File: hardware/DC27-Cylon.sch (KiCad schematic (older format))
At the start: 32 parts, among them J1 CONN_04LOCK, J2 CONN_05LOCK, U1 STM32F030K6Tx, U2 AZ1117-3.3, Y1 16MHz

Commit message: some fixes for fab
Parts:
- C1, C2, C3, C4, C5: footprint Capacitors_SMD:C_0603 -> Sparkfun_Capacitors:0603
- U2: footprint Digikey:SOT-23-3 -> Package_TO_SOT_SMD:SOT-223-3_TabPin2
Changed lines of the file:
@@
 F 0 "C3" H 1365 1396 50  0000 L CNN
 F 1 "22p" H 1365 1305 50  0000 L CNN
-F 2 "Capacitors_SMD:C_0603" H 1288 1200 50  0001 C CNN
+F 2 "Sparkfun_Capacitors:0603" H 1288 1200 50  0001 C CNN
 F 3 "~" H 1250 1350 50  0001 C CNN
 F 4 "CC0603JRNPO9BN220" H 1250 1350 50  0001 C CNN "MPN"
@@
 F 0 "C1" H 965 1396 50  0000 L CNN
 F 1 "22p" H 965 1305 50  0000 L CNN
-F 2 "Capacitors_SMD:C_0603" H 888 1200 50  0001 C CNN
+F 2 "Sparkfun_Capacitors:0603" H 888 1200 50  0001 C CNN
 F 3 "~" H 850 1350 50  0001 C CNN
 F 4 "CC0603JRNPO9BN220" H 850 1350 50  0001 C CNN "MPN"
@@
 F 0 "C2" H 1365 6096 50  0000 L CNN
 F 1 "10μ" H 1365 6005 50  0000 L CNN
-F 2 "Capacitors_SMD:C_0603" H 1288 5900 50  0001 C CNN
+F 2 "Sparkfun_Capacitors:0603" H 1288 5900 50  0001 C CNN
 F 3 "~" H 1250 6050 50  0001 C CNN
 F 4 "CL10A106KP8NNNC" H 1250 6050 50  0001 C CNN "MPN"
@@
 F 0 "C5" H 2165 6096 50  0000 L CNN
 F 1 "22p" H 2165 6005 50  0000 L CNN
-F 2 "Capacitors_SMD:C_0603" H 2088 5900 50  0001 C CNN
+F 2 "Sparkfun_Capacitors:0603" H 2088 5900 50  0001 C CNN
 F 3 "~" H 2050 6050 50  0001 C CNN
 F 4 "CC0603JRNPO9BN220" H 2050 6050 50  0001 C CNN "MPN"
@@
 F 0 "C4" H 1615 2046 50  0000 L CNN
 F 1 "22p" H 1615 1955 50  0000 L CNN
-F 2 "Capacitors_SMD:C_0603" H 1538 1850 50  0001 C CNN
+F 2 "Sparkfun_Capacitors:0603" H 1538 1850 50  0001 C CNN
 F 3 "~" H 1500 2000 50  0001 C CNN
 F 4 "CC0603JRNPO9BN220" H 1500 2000 50  0001 C CNN "MPN"
@@
 F 0 "U2" H 1700 6142 50  0000 C CNN
 F 1 "AZ1117-3.3" H 1700 6051 50  0000 C CNN
-F 2 "Digikey:SOT-23-3" H 1700 6150 50  0001 C CIN
+F 2 "Package_TO_SOT_SMD:SOT-223-3_TabPin2" H 1700 6150 50  0001 C CIN
 F 3 "https://www.diodes.com/assets/Datasheets/AZ1117.pdf" H 1700 5900 50  0001 C CNN
 F 4 "AZ1117CH-3.3TRG1" H 1700 5900 50  0001 C CNN "MPN"

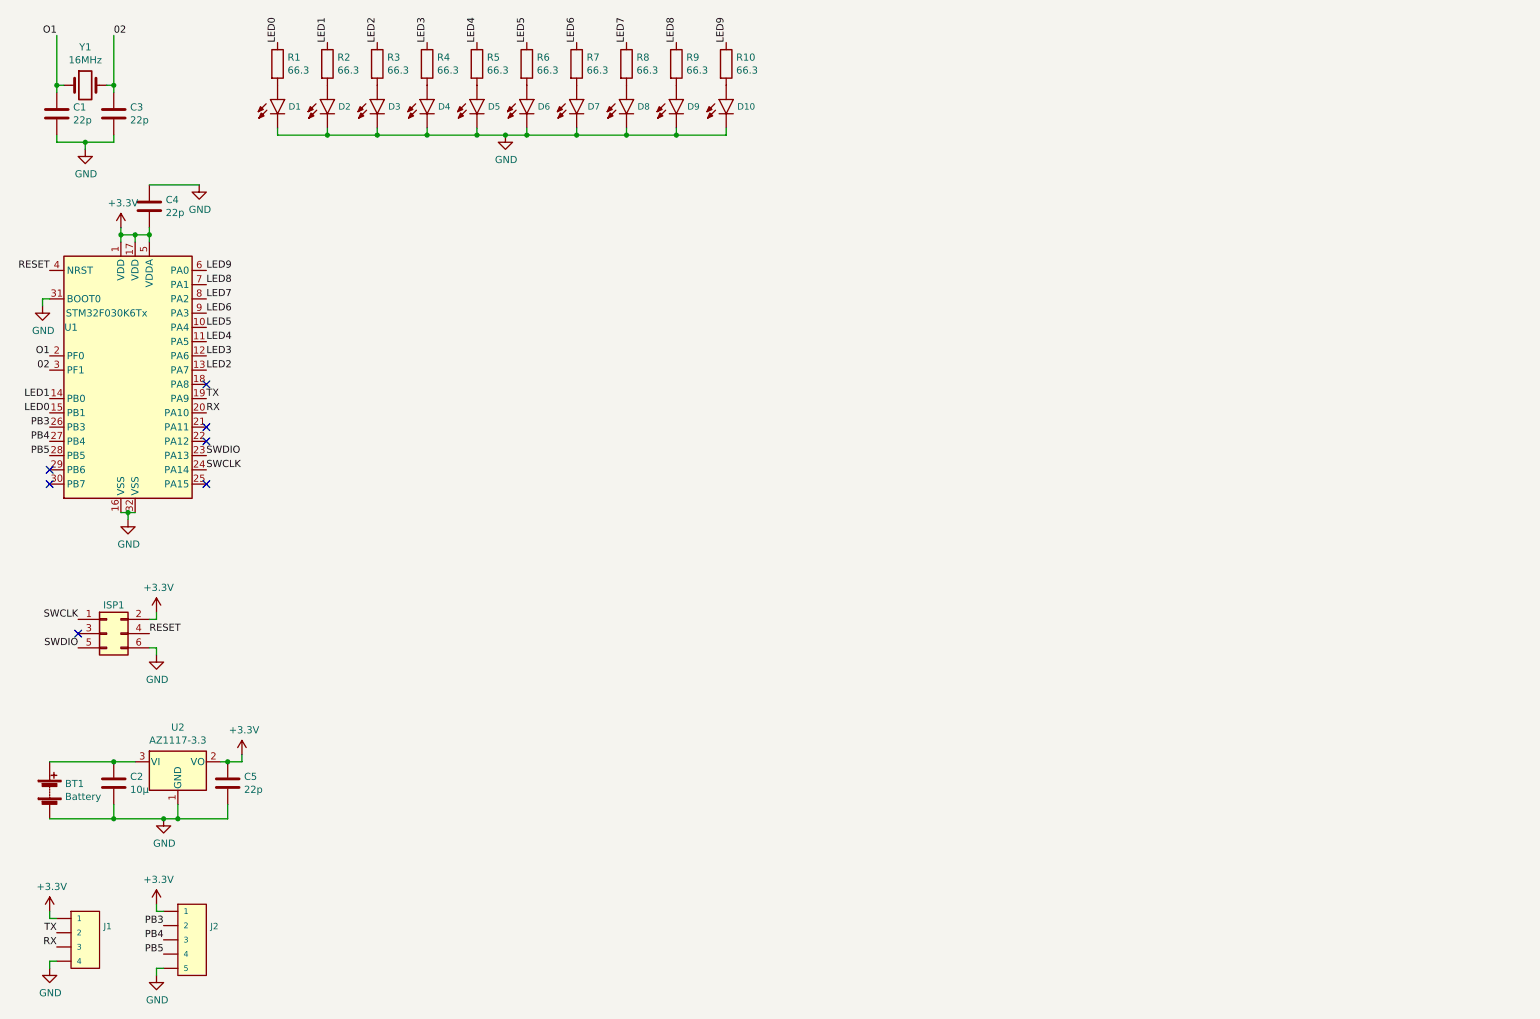
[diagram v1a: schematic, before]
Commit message: Add shift registers to address more leds, should charlieplex
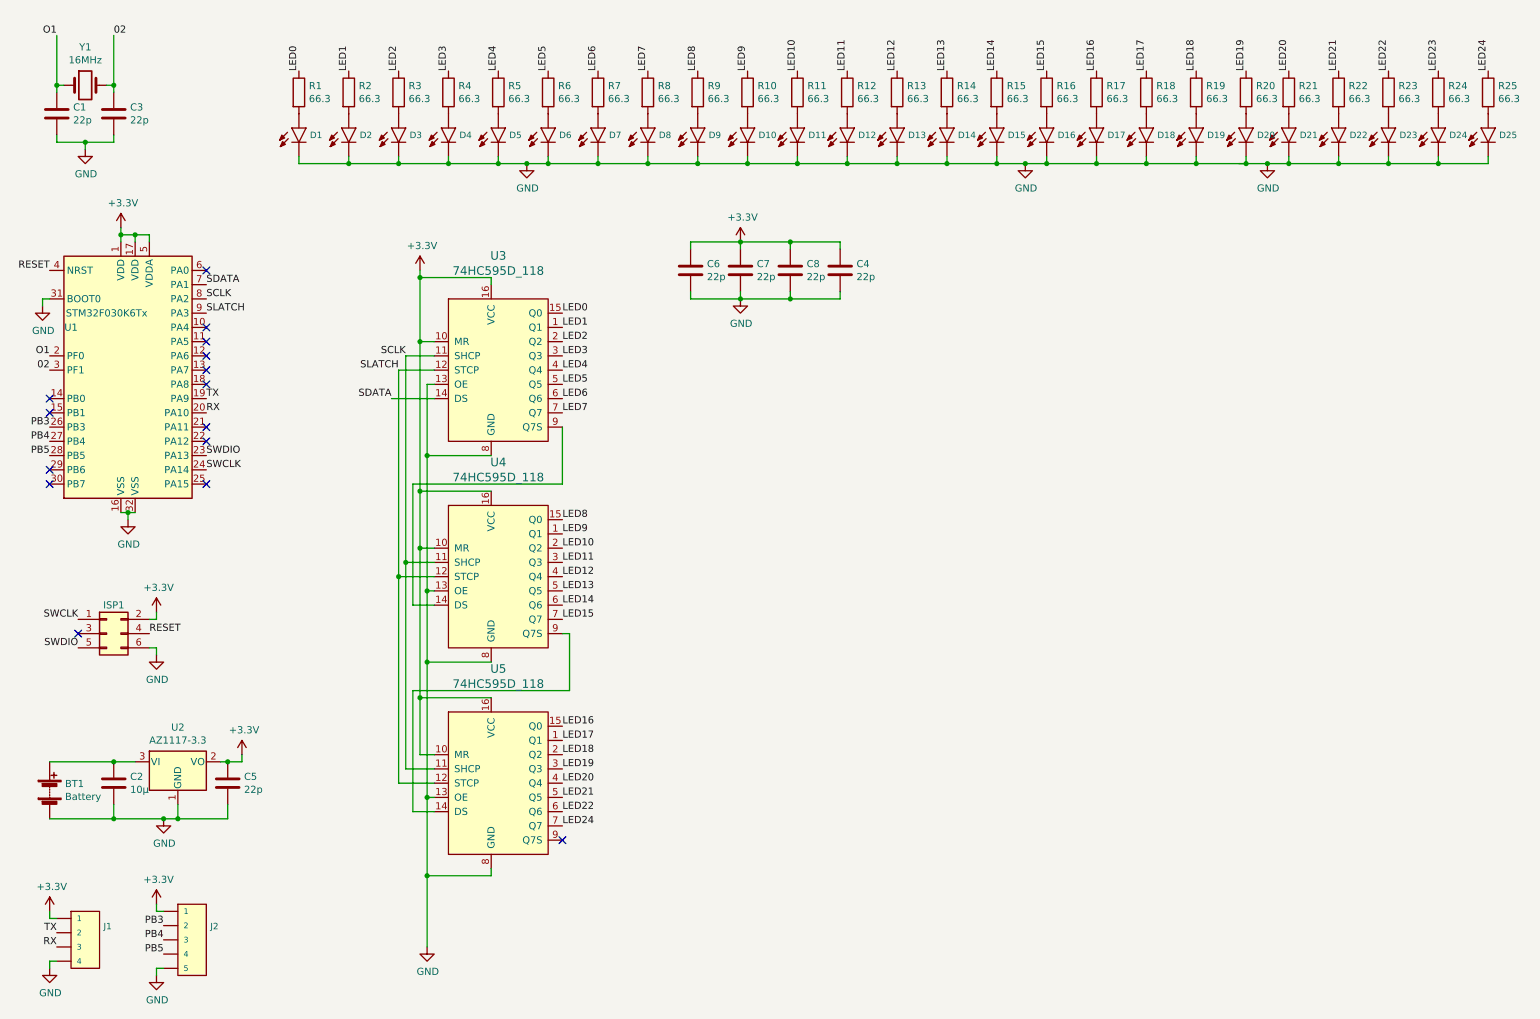
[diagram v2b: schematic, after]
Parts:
- added C6, C7, C8: 22p, Sparkfun_Capacitors:0603, symbol Device:C
- added D11, D12, D13, D14, D15, D16, D17, D18, D19, D20, D21, D22, D23, D24, D25: LED0603, Sparkfun_LED:LED-0603, symbol SparkFun-LED:LED0603
- added R11, R12, R13, R14, R15, R16, R17, R18, R19, R20, R21, R22, R23, R24, R25: 66.3, Sparkfun_Resistors:0603, symbol Device:R
- added U3, U4, U5: 74HC595D_118, Digikey:SOIC-16_W3.90mm, symbol dk_Logic-Shift-Registers:74HC595D_118
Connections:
- net +3V3: now also C4.1, C6.1, C7.1, C8.1, U3.10 (MR), U3.16 (VCC), U4.10 (MR), U4.16 (VCC), U5.10 (MR), U5.16 (VCC); no longer C4.2
- net GND: now also C4.2, C6.2, C7.2, C8.2, D11.C, D12.C, D13.C, D14.C, D15.C, D16.C, D17.C, D18.C, D19.C, D20.C, D21.C, D22.C, D23.C, D24.C, D25.C, U3.13 (OE), U3.8 (GND), U4.13 (OE), U4.8 (GND), U5.13 (OE), U5.8 (GND); no longer C4.1
- net LED0: now also U3.15 (Q0); no longer U1.15 (PB1)
- net LED1: now also U3.1 (Q1); no longer U1.14 (PB0)
- net LED2: now also U3.2 (Q2); no longer U1.13 (PA7)
- net LED3: now also U3.3 (Q3); no longer U1.12 (PA6)
- net LED4: now also U3.4 (Q4); no longer U1.11 (PA5)
- net LED5: now also U3.5 (Q5); no longer U1.10 (PA4)
- net LED6: now also U3.6 (Q6); no longer U1.9 (PA3)
- net LED7: now also U3.7 (Q7); no longer U1.8 (PA2)
- net LED8: now also U4.15 (Q0); no longer U1.7 (PA1)
- net LED9: now also U4.1 (Q1); no longer U1.6 (PA0)
- new net: D11.A, R11.2
- new net: D12.A, R12.2
- new net: D13.A, R13.2
- new net: D14.A, R14.2
- new net: D15.A, R15.2
- new net: D16.A, R16.2
- new net: D17.A, R17.2
- new net: D18.A, R18.2
- new net: D19.A, R19.2
- new net: D20.A, R20.2
- new net: D25.A, R25.2
- new net: D24.A, R24.2
- new net: D23.A, R23.2
- new net: D22.A, R22.2
- new net: D21.A, R21.2
- new net: U3.9 (Q7S), U4.14 (DS)
- new net: U4.9 (Q7S), U5.14 (DS)
- new net LED10: R11.1, U4.2 (Q2)
- new net LED11: R12.1, U4.3 (Q3)
- new net LED12: R13.1, U4.4 (Q4)
- new net LED13: R14.1, U4.5 (Q5)
- new net LED14: R15.1, U4.6 (Q6)
- new net LED15: R16.1, U4.7 (Q7)
- new net LED16: R17.1, U5.15 (Q0)
- new net LED17: R18.1, U5.1 (Q1)
- new net LED18: R19.1, U5.2 (Q2)
- new net LED19: R20.1, U5.3 (Q3)
- new net LED20: R21.1, U5.4 (Q4)
- new net LED21: R22.1, U5.5 (Q5)
- new net LED22: R23.1, U5.6 (Q6)
- new net LED23: R24.1
- new net LED24: R25.1, U5.7 (Q7)
- new net SCLK: U1.8 (PA2), U3.11 (SHCP), U4.11 (SHCP), U5.11 (SHCP)
- new net SDATA: U1.7 (PA1), U3.14 (DS)
- new net SLATCH: U1.9 (PA3), U3.12 (STCP), U4.12 (STCP), U5.12 (STCP)
- no-connect marks 7 -> 15
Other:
- moved on the sheet: C4, D1, D10, D2, D3, D4, D5, D6, D7, D8, D9, R1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

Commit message: Rough layout, still need all tracks
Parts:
- removed D24: LED0603, Sparkfun_LED:LED-0603, symbol SparkFun-LED:LED0603
- removed R24: 66.3, Sparkfun_Resistors:0603, symbol Device:R
- BT1: footprint (none) -> DC27-Cylon:BatteryHolder_Keystone_2464_3xAA
- ISP1: footprint Sparkfun_Connectors:2X3 -> DC27-Cylon:ISP_2X3
- renumbered D25 to D24, R25 to R24
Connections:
- net LED0: now also U3.7 (Q7); no longer U3.15 (Q0)
- net LED1: now also U3.6 (Q6); no longer U3.1 (Q1)
- net LED10: now also U4.5 (Q5); no longer U4.2 (Q2)
- net LED11: now also U4.4 (Q4); no longer U4.3 (Q3)
- net LED12: now also U4.3 (Q3); no longer U4.4 (Q4)
- net LED13: now also U4.2 (Q2); no longer U4.5 (Q5)
- net LED14: now also U4.1 (Q1); no longer U4.6 (Q6)
- net LED15: now also U4.15 (Q0); no longer U4.7 (Q7)
- net LED16: now also U5.7 (Q7); no longer U5.15 (Q0)
- net LED17: now also U5.6 (Q6); no longer U5.1 (Q1)
- net LED18: now also U5.5 (Q5); no longer U5.2 (Q2)
- net LED19: now also U5.4 (Q4); no longer U5.3 (Q3)
- net LED2: now also U3.5 (Q5); no longer U3.2 (Q2)
- net LED20: now also U5.3 (Q3); no longer U5.4 (Q4)
- net LED21: now also U5.2 (Q2); no longer U5.5 (Q5)
- net LED22: now also U5.1 (Q1); no longer U5.6 (Q6)
- net LED23: now also R24.1, U5.15 (Q0)
- net LED3: now also U3.4 (Q4); no longer U3.3 (Q3)
- net LED4: now also U3.3 (Q3); no longer U3.4 (Q4)
- net LED5: now also U3.2 (Q2); no longer U3.5 (Q5)
- net LED6: now also U3.1 (Q1); no longer U3.6 (Q6)
- net LED7: now also U3.15 (Q0); no longer U3.7 (Q7)
- net LED8: now also U4.7 (Q7); no longer U4.15 (Q0)
- net LED9: now also U4.6 (Q6); no longer U4.1 (Q1)
- net SCLK: now also U1.9 (PA3); no longer U1.8 (PA2)
- net SLATCH: now also U1.8 (PA2); no longer U1.9 (PA3)
- removed net LED24: R24.1, U5.7 (Q7)
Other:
- moved on the sheet: D24, R24
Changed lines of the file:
@@
 F 0 "BT1" H 908 6146 50  0000 L CNN
 F 1 "Battery" H 908 6055 50  0000 L CNN
-F 2 "" V 800 6160 50  0001 C CNN
+F 2 "DC27-Cylon:BatteryHolder_Keystone_2464_3xAA" V 800 6160 50  0001 C CNN
 F 3 "~" V 800 6160 50  0001 C CNN
 F 4 "DNP" H 800 6100 50  0001 C CNN "MPN"
@@
 F 0 "ISP1" H 1250 5200 50  0000 C CNN
 F 1 "ISP" H 1250 4800 50  0001 C CNN
-F 2 "Sparkfun_Connectors:2X3" H 1200 5000 50  0001 C CNN
+F 2 "DC27-Cylon:ISP_2X3" H 1200 5000 50  0001 C CNN
 F 3 "~" H 1200 5000 50  0001 C CNN
 F 4 "DNP" H 1200 5000 50  0001 C CNN "MPN"
@@
 $EndComp
 $Comp
-L SparkFun-LED:LED0603 D25
+L SparkFun-LED:LED0603 D24
 U 1 1 5D1DA41C
-P 10900 1450
-F 0 "D25" H 10977 1400 45  0000 L CNN
-F 1 "LED0603" H 10978 1411 45  0001 L CNN
-F 2 "Sparkfun_LED:LED-0603" V 10700 1450 20  0001 C CNN
-F 3 "" H 10900 1450 50  0001 C CNN
-F 4 "XXX-00000" H 10978 1316 60  0001 L CNN "Field4"
-F 5 "ORH-R36G" H 10900 1450 50  0001 C CNN "MPN"
-F 6 "Orient" H 10900 1450 50  0001 C CNN "Manufacturer"
-F 7 "10351" H 10900 1450 50  0001 C CNN "OPL#"
-	1    10900 1450
-	1    0    0    -1
-$EndComp
-$Comp
-L SparkFun-LED:LED0603 D24
-U 1 1 5D1DA42A
 P 10550 1450
 F 0 "D24" H 10627 1400 45  0000 L CNN
@@
 	1    0    0    -1
 $EndComp
-Text Label 10900 1050 1    50   ~ 0
-LED24
 Text Label 10550 1050 1    50   ~ 0
 LED23
@@
 LED20
 $Comp
-L Device:R R25
+L Device:R R24
 U 1 1 5D1DA466
-P 10900 1200
-F 0 "R25" H 10970 1246 50  0000 L CNN
-F 1 "66.3" H 10970 1155 50  0000 L CNN
-F 2 "Sparkfun_Resistors:0603" V 10830 1200 50  0001 C CNN
-F 3 "~" H 10900 1200 50  0001 C CNN
-F 4 "RC0603FR-0766K5L" H 10900 1200 50  0001 C CNN "MPN"
-F 5 "Yageo" H 10900 1200 50  0001 C CNN "Manufacturer"
-F 6 "818" H 10900 1200 50  0001 C CNN "OPL#"
-	1    10900 1200
-	1    0    0    -1
-$EndComp
-$Comp
-L Device:R R24
-U 1 1 5D1DA473
 P 10550 1200
 F 0 "R24" H 10620 1246 50  0000 L CNN
@@
 	9850 1650 9850 1700
 Wire Wire Line
-	10200 1700 10550 1700
-Connection ~ 10200 1700
-Wire Wire Line
 	10200 1650 10200 1700
-Wire Wire Line
-	10550 1700 10900 1700
-Connection ~ 10550 1700
-Wire Wire Line
-	10550 1650 10550 1700
-Wire Wire Line
-	10900 1700 10900 1650
 $Comp
 L power:GND #PWR0116
@@
 Connection ~ 6050 1700
 Connection ~ 5700 1700
+Text Label 4400 3450 0    50   ~ 0
+LED0
+Text Label 4400 3350 0    50   ~ 0
+LED1
+Text Label 4400 3250 0    50   ~ 0
+LED2
+Text Label 4400 3150 0    50   ~ 0
+LED3
+Text Label 4400 3050 0    50   ~ 0
+LED4
+Text Label 4400 2950 0    50   ~ 0
+LED5
+Text Label 4400 2850 0    50   ~ 0
+LED6
 Text Label 4400 2750 0    50   ~ 0
-LED0
-Text Label 4400 2850 0    50   ~ 0
-LED1
-Text Label 4400 2950 0    50   ~ 0
-LED2
-Text Label 4400 3050 0    50   ~ 0
-LED3
-Text Label 4400 3150 0    50   ~ 0
-LED4
-Text Label 4400 3250 0    50   ~ 0
-LED5
-Text Label 4400 3350 0    50   ~ 0
-LED6
-Text Label 4400 3450 0    50   ~ 0
 LED7
-Text Label 4400 4200 0    50   ~ 0
+Text Label 4400 4900 0    50   ~ 0
 LED8
 Text Label 5700 1050 1    50   ~ 0
 LED9
+Text Label 4400 4800 0    50   ~ 0
+LED9
+Text Label 4400 4700 0    50   ~ 0
+LED10
+Text Label 4400 4600 0    50   ~ 0
+LED11
+Text Label 4400 4500 0    50   ~ 0
+LED12
+Text Label 4400 4400 0    50   ~ 0
+LED13
 Text Label 4400 4300 0    50   ~ 0
-LED9
-Text Label 4400 4400 0    50   ~ 0
-LED10
-Text Label 4400 4500 0    50   ~ 0
-LED11
-Text Label 4400 4600 0    50   ~ 0
-LED12
-Text Label 4400 4700 0    50   ~ 0
-LED13
-Text Label 4400 4800 0    50   ~ 0
 LED14
-Text Label 4400 4900 0    50   ~ 0
+Text Label 4400 4200 0    50   ~ 0
 LED15
-Text Label 4400 5650 0    50   ~ 0
-LED16
-Text Label 4400 5750 0    50   ~ 0
-LED17
-Text Label 4400 5850 0    50   ~ 0
-LED18
-Text Label 4400 5950 0    50   ~ 0
-LED19
-Text Label 4400 6050 0    50   ~ 0
-LED20
-Text Label 4400 6150 0    50   ~ 0
-LED21
-Text Label 4400 6250 0    50   ~ 0
-LED22
-Text Label 4400 6350 0    50   ~ 0
-LED24
 $Comp
 L power:GND #PWR0117
@@
 Text Label 1900 2550 0    50   ~ 0
 SDATA
+Text Label 1900 2750 0    50   ~ 0
+SCLK
 Text Label 1900 2650 0    50   ~ 0
-SCLK
-Text Label 1900 2750 0    50   ~ 0
 SLATCH
 NoConn ~ 800  3350
@@
 	4400 5000 4450 5000
 Wire Wire Line
-	4450 5000 4450 5400
-Wire Wire Line
-	4450 5400 3350 5400
-Wire Wire Line
 	3350 5400 3350 6250
 Wire Wire Line
@@
 	6350 2650 6000 2650
 Connection ~ 6000 2650
+Wire Wire Line
+	10550 1650 10550 1700
+Wire Wire Line
+	10550 1700 10200 1700
+Connection ~ 10200 1700
+Wire Wire Line
+	4450 5400 3350 5400
+Wire Wire Line
+	4450 5000 4450 5400
+Text Label 4400 5650 0    50   ~ 0
+LED23
+Text Label 4400 5750 0    50   ~ 0
+LED22
+Text Label 4400 5850 0    50   ~ 0
+LED21
+Text Label 4400 5950 0    50   ~ 0
+LED20
+Text Label 4400 6050 0    50   ~ 0
+LED19
+Text Label 4400 6150 0    50   ~ 0
+LED18
+Text Label 4400 6250 0    50   ~ 0
+LED17
+Text Label 4400 6350 0    50   ~ 0
+LED16
 $EndSCHEMATC

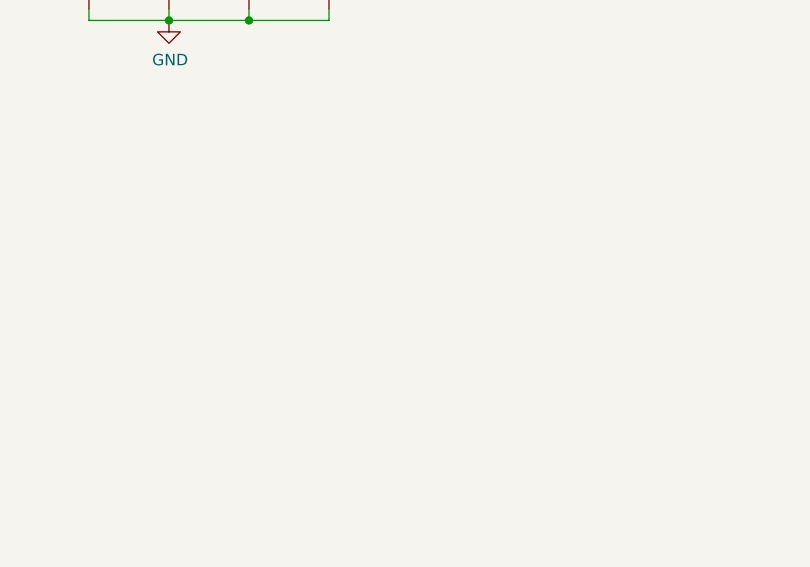
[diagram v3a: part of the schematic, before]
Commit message: Add SAO to head
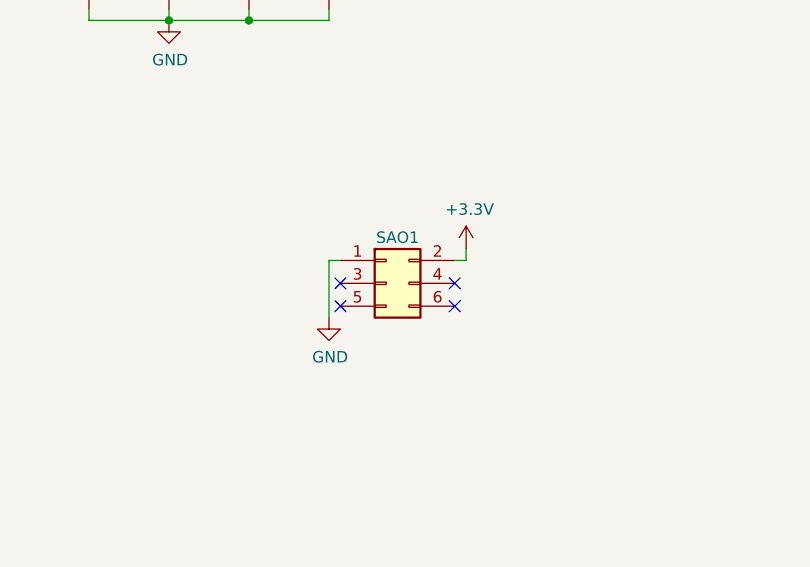
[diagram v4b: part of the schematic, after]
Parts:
- added SAO1: SAO, Sparkfun_Connectors:2X3, symbol Connector_Generic:Conn_02x03_Odd_Even
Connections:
- net +3V3: now also SAO1.2 (Pin_2)
- net GND: now also SAO1.1 (Pin_1)
- no-connect marks 15 -> 19
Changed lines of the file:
@@
 Text Label 4400 6350 0    50   ~ 0
 LED16
+$Comp
+L Connector_Generic:Conn_02x03_Odd_Even SAO1
+U 1 1 5D16439E
+P 6600 3800
+F 0 "SAO1" H 6650 4000 50  0000 C CNN
+F 1 "SAO" H 6650 3600 50  0001 C CNN
+F 2 "Sparkfun_Connectors:2X3" H 6600 3800 50  0001 C CNN
+F 3 "~" H 6600 3800 50  0001 C CNN
+F 4 "DNP" H 6600 3800 50  0001 C CNN "MPN"
+F 5 "N/A" H 6600 3800 50  0001 C CNN "Manufacturer"
+F 6 "DNP" H 6600 3800 50  0001 C CNN "OPL#"
+	1    6600 3800
+	1    0    0    -1
+$EndComp
+$Comp
+L power:+3.3V #PWR?
+U 1 1 5D17A727
+P 6950 3650
+F 0 "#PWR?" H 6950 3500 50  0001 C CNN
+F 1 "+3.3V" H 6965 3823 50  0000 C CNN
+F 2 "" H 6950 3650 50  0001 C CNN
+F 3 "" H 6950 3650 50  0001 C CNN
+	1    6950 3650
+	1    0    0    -1
+$EndComp
+$Comp
+L power:GND #PWR?
+U 1 1 5D17D9AC
+P 6350 3950
+F 0 "#PWR?" H 6350 3700 50  0001 C CNN
+F 1 "GND" H 6355 3777 50  0000 C CNN
+F 2 "" H 6350 3950 50  0001 C CNN
+F 3 "" H 6350 3950 50  0001 C CNN
+	1    6350 3950
+	1    0    0    -1
+$EndComp
+Wire Wire Line
+	6350 3700 6400 3700
+Wire Wire Line
+	6950 3700 6900 3700
+NoConn ~ 6400 3800
+NoConn ~ 6900 3800
+NoConn ~ 6900 3900
+NoConn ~ 6400 3900
+Wire Wire Line
+	6950 3650 6950 3700
+Wire Wire Line
+	6350 3950 6350 3700
 $EndSCHEMATC
